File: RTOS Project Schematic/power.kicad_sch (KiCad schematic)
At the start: 4 parts, among them U4 LM2596S-ADJ, U5 LM2596S-ADJ, U6 LM2596S-ADJ

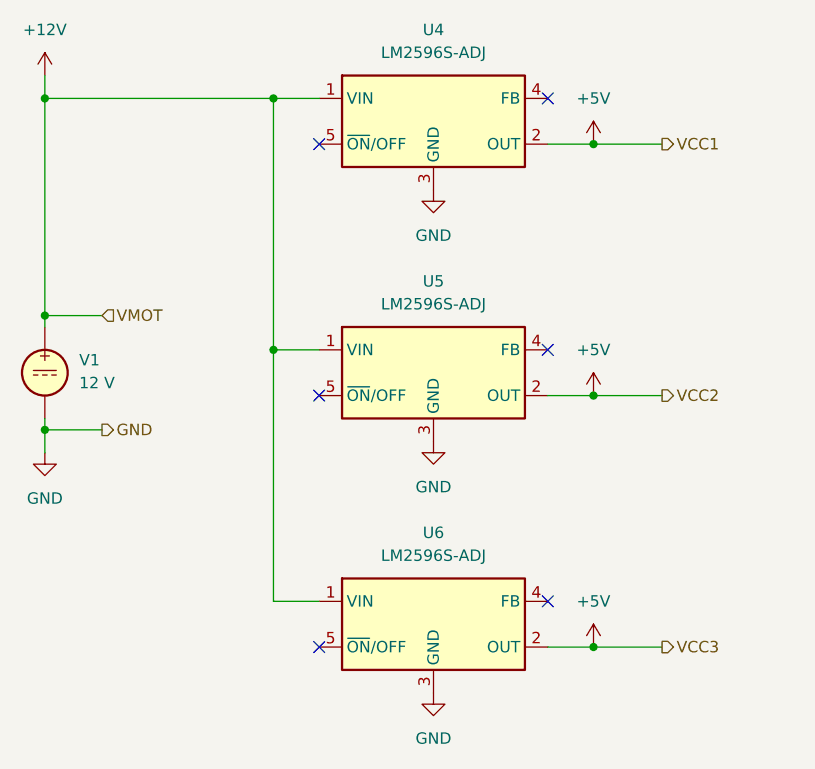
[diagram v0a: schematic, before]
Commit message: Updated power rails
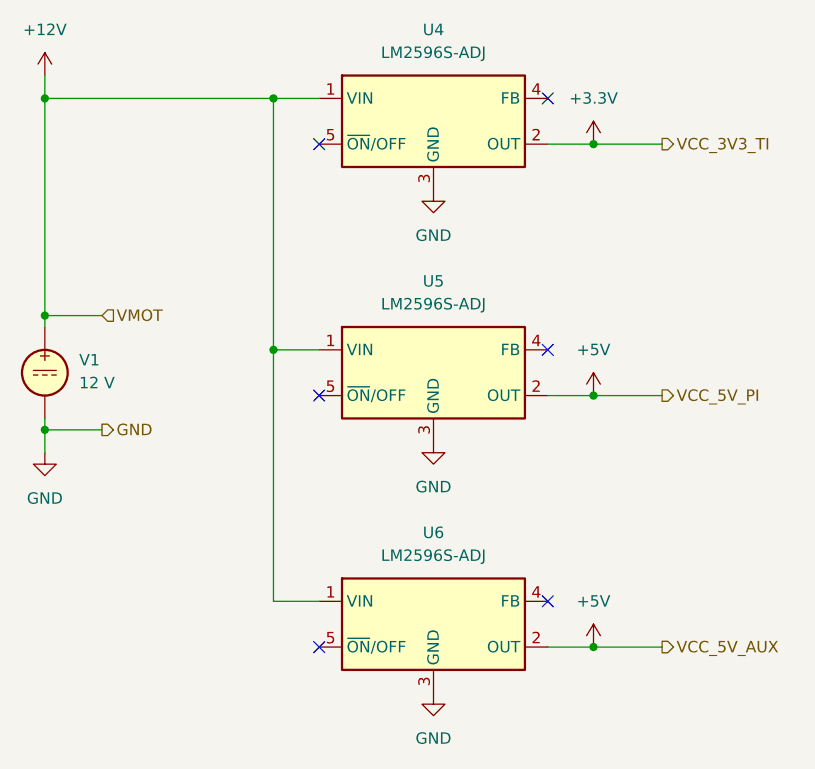
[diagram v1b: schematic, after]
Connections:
- net +5V: no longer U4.2 (OUT)
- new net +3.3V: U4.2 (OUT)
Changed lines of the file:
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@@
   (junction (at 92.71 72.39) (diameter 0) (color 0 0 0 0)
   )
+  (junction (at 153.67 53.34) (diameter 0) (color 0 0 0 0)
+  )
   (junction (at 118.11 48.26) (diameter 0) (color 0 0 0 0)
-  )
-  (junction (at 153.67 53.34) (diameter 0) (color 0 0 0 0)
   )
   (junction (at 92.71 85.09) (diameter 0) (color 0 0 0 0)
@@
     (stroke (width 0) (type default))
   )
+  (wire (pts (xy 153.67 81.28) (xy 161.29 81.28))
+    (stroke (width 0) (type default))
+  )
+  (wire (pts (xy 92.71 73.66) (xy 92.71 72.39))
+    (stroke (width 0) (type default))
+  )
   (wire (pts (xy 153.67 53.34) (xy 161.29 53.34))
     (stroke (width 0) (type default))
   )
-  (wire (pts (xy 153.67 81.28) (xy 161.29 81.28))
-    (stroke (width 0) (type default))
-  )
-  (wire (pts (xy 92.71 73.66) (xy 92.71 72.39))
-    (stroke (width 0) (type default))
-  )
   (wire (pts (xy 123.19 76.2) (xy 118.11 76.2))
     (stroke (width 0) (type default))
@@
     (effects (font (size 1.27 1.27)) (justify left))
   )
-  (hierarchical_label "VCC3" (shape output) (at 161.29 109.22 0) (fields_autoplaced)
-    (effects (font (size 1.27 1.27)) (justify left))
-  )
-  (hierarchical_label "VCC1" (shape output) (at 161.29 53.34 0) (fields_autoplaced)
-    (effects (font (size 1.27 1.27)) (justify left))
-  )
-  (hierarchical_label "VCC2" (shape output) (at 161.29 81.28 0) (fields_autoplaced)
+  (hierarchical_label "VCC_5V_AUX" (shape output) (at 161.29 109.22 0) (fields_autoplaced)
+    (effects (font (size 1.27 1.27)) (justify left))
+  )
+  (hierarchical_label "VCC_3V3_TI" (shape output) (at 161.29 53.34 0) (fields_autoplaced)
+    (effects (font (size 1.27 1.27)) (justify left))
+  )
+  (hierarchical_label "VCC_5V_PI" (shape output) (at 161.29 81.28 0) (fields_autoplaced)
     (effects (font (size 1.27 1.27)) (justify left))
   )
@@
     )
   )
-  (symbol (lib_id "power:+5V") (at 153.67 53.34 0) (unit 1)
-    (in_bom yes) (on_board yes) (dnp no) (fields_autoplaced)
-    (property "Reference" "#PWR02" (at 153.67 57.15 0)
-      (effects (font (size 1.27 1.27)) hide)
-    )
-    (property "Value" "+5V" (at 153.67 48.26 0)
+  (symbol (lib_id "power:+3.3V") (at 153.67 53.34 0) (unit 1)
+    (in_bom yes) (on_board yes) (dnp no) (fields_autoplaced)
+    (property "Reference" "#PWR07" (at 153.67 57.15 0)
+      (effects (font (size 1.27 1.27)) hide)
+    )
+    (property "Value" "+3.3V" (at 153.67 48.26 0)
       (effects (font (size 1.27 1.27)))
     )
@@
       (project "RTOS Project Schematic"
         (path "/c6d2ace8-9811-4d31-9242-ec8aa6e12e77/e60e34ae-ed22-4cae-87b4-3966c5ed0e25"
-          (reference "#PWR02") (unit 1)
-        )
-      )
+          (reference "#PWR07") (unit 1)
+        )
+      )

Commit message: Added preliminary microphone circuit
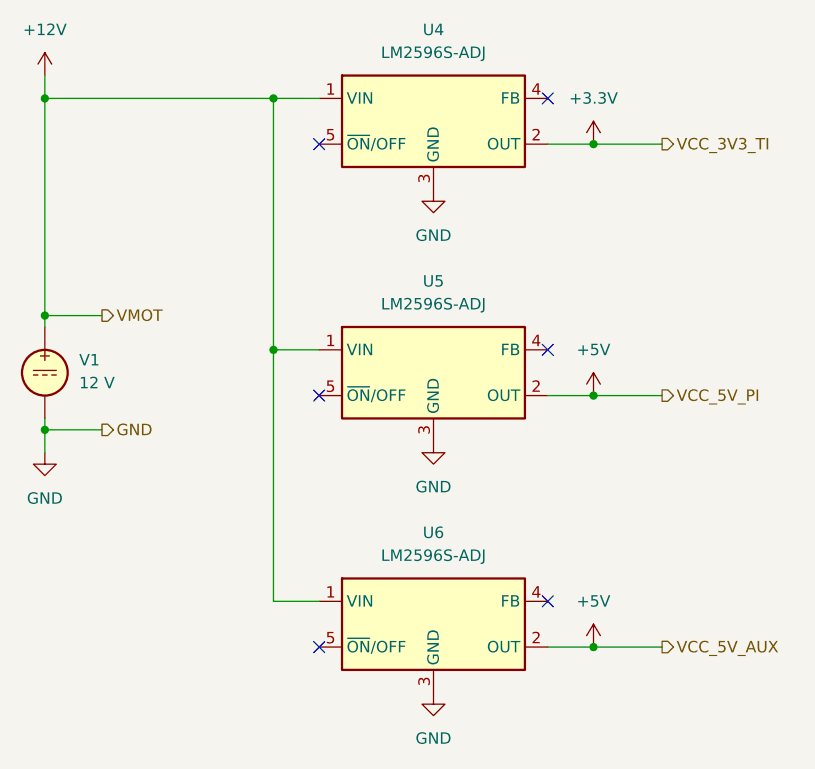
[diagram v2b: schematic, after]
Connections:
- net +5V renamed +5V_A
- net +5V_A: no longer U6.2 (OUT)
- new net +5V_B: U6.2 (OUT)
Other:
- company: (none) -> Eddie and Felix
- title: (none) -> Power
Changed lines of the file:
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@@
 (kicad_sch (version 20230121) (generator eeschema)
   (paper "A4")
+  (title_block
+    (title "Power")
+    (date "2023-11-29")
+    (rev "A")
+    (company "Eddie and Felix")
+  )
+  (junction (at 153.67 81.28) (diameter 0) (color 0 0 0 0)
+  )
+  (junction (at 118.11 76.2) (diameter 0) (color 0 0 0 0)
+  )
+  (junction (at 92.71 72.39) (diameter 0) (color 0 0 0 0)
+  )
+  (junction (at 153.67 53.34) (diameter 0) (color 0 0 0 0)
+  )
   (junction (at 153.67 109.22) (diameter 0) (color 0 0 0 0)
-  )
-  (junction (at 153.67 81.28) (diameter 0) (color 0 0 0 0)
-  )
-  (junction (at 118.11 76.2) (diameter 0) (color 0 0 0 0)
-  )
-  (junction (at 92.71 72.39) (diameter 0) (color 0 0 0 0)
-  )
-  (junction (at 153.67 53.34) (diameter 0) (color 0 0 0 0)
   )
   (junction (at 118.11 48.26) (diameter 0) (color 0 0 0 0)
@@
     (stroke (width 0) (type default))
   )
+  (wire (pts (xy 148.59 81.28) (xy 153.67 81.28))
+    (stroke (width 0) (type default))
+  )
+  (wire (pts (xy 92.71 73.66) (xy 92.71 72.39))
+    (stroke (width 0) (type default))
+  )
+  (wire (pts (xy 153.67 53.34) (xy 161.29 53.34))
+    (stroke (width 0) (type default))
+  )
+  (wire (pts (xy 123.19 76.2) (xy 118.11 76.2))
+    (stroke (width 0) (type default))
+  )
+  (wire (pts (xy 118.11 48.26) (xy 118.11 76.2))
+    (stroke (width 0) (type default))
+  )
+  (wire (pts (xy 92.71 85.09) (xy 92.71 83.82))
+    (stroke (width 0) (type default))
+  )
   (wire (pts (xy 153.67 81.28) (xy 161.29 81.28))
     (stroke (width 0) (type default))
   )
-  (wire (pts (xy 92.71 73.66) (xy 92.71 72.39))
-    (stroke (width 0) (type default))
-  )
-  (wire (pts (xy 153.67 53.34) (xy 161.29 53.34))
-    (stroke (width 0) (type default))
-  )
-  (wire (pts (xy 123.19 76.2) (xy 118.11 76.2))
-    (stroke (width 0) (type default))
-  )
-  (wire (pts (xy 118.11 48.26) (xy 118.11 76.2))
-    (stroke (width 0) (type default))
-  )
-  (wire (pts (xy 148.59 81.28) (xy 153.67 81.28))
-    (stroke (width 0) (type default))
-  )
-  (wire (pts (xy 92.71 85.09) (xy 92.71 83.82))
-    (stroke (width 0) (type default))
-  )
   (wire (pts (xy 148.59 109.22) (xy 153.67 109.22))
     (stroke (width 0) (type default))
   )
+  (wire (pts (xy 153.67 109.22) (xy 161.29 109.22))
+    (stroke (width 0) (type default))
+  )
   (wire (pts (xy 148.59 53.34) (xy 153.67 53.34))
     (stroke (width 0) (type default))
@@
     (stroke (width 0) (type default))
   )
-  (wire (pts (xy 153.67 109.22) (xy 161.29 109.22))
-    (stroke (width 0) (type default))
-  )
   (wire (pts (xy 118.11 48.26) (xy 123.19 48.26))
     (stroke (width 0) (type default))
   )
-  (hierarchical_label "VMOT" (shape input) (at 99.06 72.39 0) (fields_autoplaced)
+  (hierarchical_label "VMOT" (shape output) (at 99.06 72.39 0) (fields_autoplaced)
     (effects (font (size 1.27 1.27)) (justify left))
   )
@@
     )
   )
-  (symbol (lib_id "power:+5V") (at 153.67 109.22 0) (unit 1)
-    (in_bom yes) (on_board yes) (dnp no) (fields_autoplaced)
-    (property "Reference" "#PWR0102" (at 153.67 113.03 0)
-      (effects (font (size 1.27 1.27)) hide)
-    )
-    (property "Value" "+5V" (at 153.67 104.14 0)
-      (effects (font (size 1.27 1.27)))
-    )
-    (property "Footprint" "" (at 153.67 109.22 0)
-      (effects (font (size 1.27 1.27)) hide)
-    )
-    (property "Datasheet" "" (at 153.67 109.22 0)
-      (effects (font (size 1.27 1.27)) hide)
-    )
-    (pin "1")
-    (instances
-      (project "RTOS Project Schematic"
-        (path "/c6d2ace8-9811-4d31-9242-ec8aa6e12e77/e60e34ae-ed22-4cae-87b4-3966c5ed0e25"
-          (reference "#PWR0102") (unit 1)
-        )
-      )
-    )
-  )
   (symbol (lib_id "power:+12V") (at 92.71 45.72 0) (unit 1)
     (in_bom yes) (on_board yes) (dnp no) (fields_autoplaced)
@@
         (path "/c6d2ace8-9811-4d31-9242-ec8aa6e12e77/e60e34ae-ed22-4cae-87b4-3966c5ed0e25"
           (reference "#PWR01") (unit 1)
-        )
-      )
-    )
-  )
-  (symbol (lib_id "power:+5V") (at 153.67 81.28 0) (unit 1)
-    (in_bom yes) (on_board yes) (dnp no) (fields_autoplaced)
-    (property "Reference" "#PWR03" (at 153.67 85.09 0)
-      (effects (font (size 1.27 1.27)) hide)
-    )
-    (property "Value" "+5V" (at 153.67 76.2 0)
-      (effects (font (size 1.27 1.27)))
-    )
-    (property "Footprint" "" (at 153.67 81.28 0)
-      (effects (font (size 1.27 1.27)) hide)
-    )
-    (property "Datasheet" "" (at 153.67 81.28 0)
-      (effects (font (size 1.27 1.27)) hide)
-    )
-    (pin "1")
-    (instances
-      (project "RTOS Project Schematic"
-        (path "/c6d2ace8-9811-4d31-9242-ec8aa6e12e77/e60e34ae-ed22-4cae-87b4-3966c5ed0e25"
-          (reference "#PWR03") (unit 1)
         )
       )
@@
     )
   )
+  (symbol (lib_id "power:+5V") (at 153.67 81.28 0) (unit 1)
+    (in_bom yes) (on_board yes) (dnp no) (fields_autoplaced)
+    (property "Reference" "#PWR03" (at 153.67 85.09 0)
+      (effects (font (size 1.27 1.27)) hide)
+    )
+    (property "Value" "+5V" (at 153.67 76.2 0)
+      (effects (font (size 1.27 1.27)))
+    )
+    (property "Footprint" "" (at 153.67 81.28 0)
+      (effects (font (size 1.27 1.27)) hide)
+    )
+    (property "Datasheet" "" (at 153.67 81.28 0)
+      (effects (font (size 1.27 1.27)) hide)
+    )
+    (pin "1")
+    (instances
+      (project "RTOS Project Schematic"
+        (path "/c6d2ace8-9811-4d31-9242-ec8aa6e12e77/e60e34ae-ed22-4cae-87b4-3966c5ed0e25"
+          (reference "#PWR03") (unit 1)
+        )
+      )
+    )
+  )
   (symbol (lib_id "power:GND") (at 135.89 58.42 0) (unit 1)
     (in_bom yes) (on_board yes) (dnp no) (fields_autoplaced)
-    (property "Reference" "#PWR04" (at 135.89 64.77 0)
+    (property "Reference" "#PWR010" (at 135.89 64.77 0)
       (effects (font (size 1.27 1.27)) hide)
     )
@@
       (effects (font (size 1.27 1.27)) hide)
     )
+    (pin "1")
+    (instances
+      (project "RTOS Project Schematic"
+        (path "/c6d2ace8-9811-4d31-9242-ec8aa6e12e77/e60e34ae-ed22-4cae-87b4-3966c5ed0e25"
+          (reference "#PWR010") (unit 1)
+        )
+      )
+    )
+  )
+  (symbol (lib_name "+5V_1") (lib_id "power:+5V") (at 153.67 109.22 0) (unit 1)
+    (in_bom yes) (on_board yes) (dnp no) (fields_autoplaced)
+    (property "Reference" "#PWR04" (at 153.67 113.03 0)
+      (effects (font (size 1.27 1.27)) hide)
+    )
+    (property "Value" "+5V" (at 153.67 104.14 0)
+      (effects (font (size 1.27 1.27)))
+    )
+    (property "Footprint" "" (at 153.67 109.22 0)
+      (effects (font (size 1.27 1.27)) hide)
+    )
+    (property "Datasheet" "" (at 153.67 109.22 0)
+      (effects (font (size 1.27 1.27)) hide)
+    )
